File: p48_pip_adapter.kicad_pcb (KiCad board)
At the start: 4 copper layers, 11.1 x 32.4 mm, 20 parts, among them J1 XLR3, Q1 MMBT3904, Q2 MMBT3906, Q3 MMBT3906

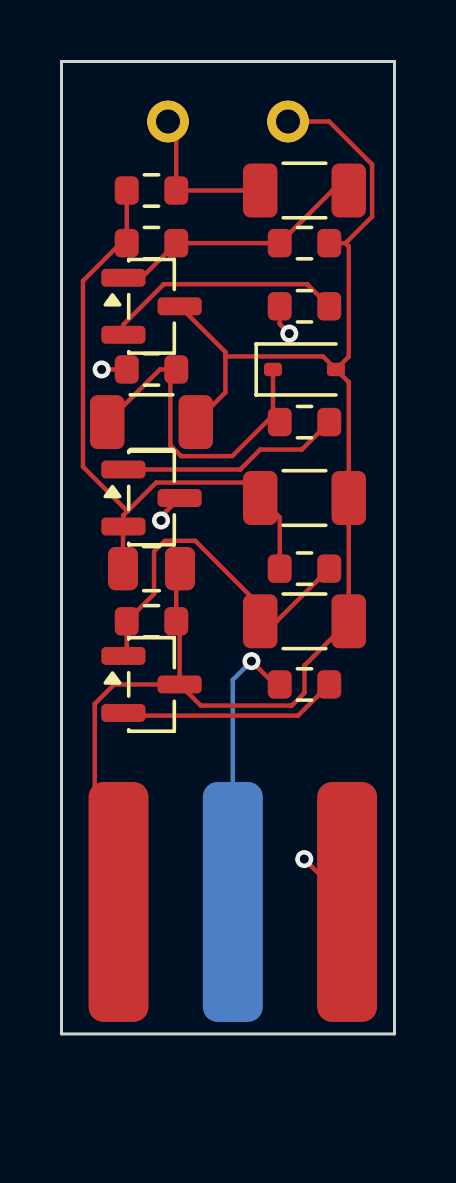
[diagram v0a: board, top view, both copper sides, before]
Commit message: rev-E board phase: real 4-layer GND planes, Power netclass, schematic-free
Turn the 4-layer stackup into a genuine ground shield (git.koti #1) and make the
documented Power netclass real (#7); regenerate every artifact for rev-E.

Board (build_pcb.py):
- In1.Cu + In2.Cu are now solid GND planes; F.Cu/B.Cu are GND-poured after
  routing. A GND via grid stitches all four layers and a fanout via ties each
  GND pad to the planes, so the uV front end sits in an on-board Faraday cage.
- Real 0.25 mm "Power" netclass for P2/P3/VPIP/VREF, persisted to the project
  file so it survives route.py's board reload into the DSN.

Routing (route.py):
- Relabel In1/In2 as Specctra 'power' layers so signal routing stays on the
  outer copper and the planes stay unbroken; flood F.Cu/B.Cu with GND and
  refill after SES import; dedupe re-emitted stitch vias.

Placement (netlist.py):
- Cluster each output stage's CB/RB emitter-bypass beside its Q/R -- a routing
  win on the now 2-signal-layer board and tighter low-noise bypass loops.

Schematic-free cleanup:
- Remove the stale hand-drawn p48_pip_adapter.kicad_sch (no generator existed;
  it had drifted to 20 vs 24 parts). Correct the false "generated from netlist"
  claims in README/SPEC: the board is synthesized from netlist.py and the
  schematic figure (gen_schematic.py) is drawn from it, so they cannot disagree.

Artifacts + docs refreshed to rev-E:
- Rerouted board (DRC 0 errors / 0 unconnected), gerbers+drill+zip, fit-test
  STL, board/connector/schematic renders. schematic.webp gains the CB/RB
  emitter-bypass network + updated values (R1 7.5k, R8 1k, R9 47k, C4 47uF).
- README/SPEC/sim: dual-GND stackup, 35.3 mm length, rev-E BOM, sim result
  tables (Zout 78 ohm, gain -0.56 dB, balanced 3.0 mA). Sim stays green (17/17).

Co-Authored-By: Claude Opus 4.8 (1M context) <noreply@anthropic.com>
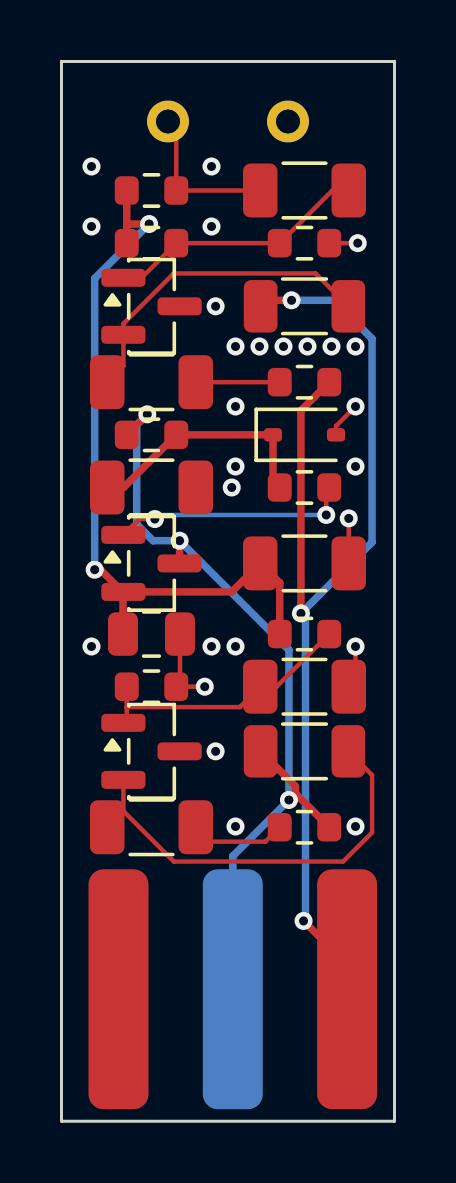
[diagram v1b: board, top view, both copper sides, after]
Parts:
- added CB2: 22uF, C_1206_3216Metric, F.Cu at (3.00, 10.7)
- added CB3: 22uF, C_1206_3216Metric, F.Cu at (3.00, 25.5)
- added RB2: 47, R_0603_1608Metric, F.Cu at (8.10, 10.7)
- added RB3: 47, R_0603_1608Metric, F.Cu at (8.10, 25.5)
- C4: value 22uF -> 47uF
- R1: value 10k -> 7.5k; footprint R_0603_1608Metric -> R_1206_3216Metric
- R2: footprint R_0603_1608Metric -> R_1206_3216Metric
- R8: value 10k -> 1k
- R9: value 100k -> 47k
- moved J1 2.91 mm to (5.55, 30.9)
- moved Q3 2.23 mm to (3.00, 23.0)
- moved R2 2.23 mm to (8.10, 23.0)
- moved C1 2.18 mm to (8.10, 16.7)
- moved C3 2.18 mm to (8.10, 20.8)
- moved C5 2.18 mm to (3.00, 19.1)
- moved Q1 2.18 mm to (3.00, 16.7)
- moved R6 2.18 mm to (8.10, 19.1)
- moved R7 2.18 mm to (3.00, 20.8)
- moved C4 2.18 mm to (3.00, 14.2)
- moved D1 2.18 mm to (8.10, 12.4)
- moved R8 2.18 mm to (8.10, 14.2)
- moved R9 2.18 mm to (3.00, 12.4)
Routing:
- net GND: track 50.3 -> 7.78 mm, vias 0 -> 26
- net P2: track 20.8 -> 35.8 mm, vias 2 -> 3
- net Q3E: track 7.33 -> 14.2 mm
- net P3: track 23.2 -> 28.2 mm
- net VREF: track 11.6 -> 8.10 mm
- net VPIP: track 21.7 -> 25.0 mm, vias 0 -> 2
- net NB3: track 0.00 -> 3.20 mm
- net Q3B: track 12.0 -> 9.01 mm
- net NB2: track 0.00 -> 2.80 mm
- net Q2E: track 8.07 -> 10.8 mm
- net Q1B: track 7.52 -> 7.99 mm, vias 0 -> 2
- added copper zone on B.Cu, net GND
- added copper zone on F.Cu, net GND
- added copper zone on In1.Cu, net GND
- added copper zone on In2.Cu, net GND
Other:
- board size 11.1 x 32.4 mm -> 11.1 x 35.3 mm
